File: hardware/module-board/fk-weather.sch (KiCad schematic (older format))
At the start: 68 parts, among them J1 MICRO-USB, J10 Conn_01x06, J11 Conn_01x06, J3 Conn_01x10, J6 CONN-HDR-2x5, M1 MOUNT_HOLE, M2 MOUNT_HOLE, M3 MOUNT_HOLE, M4 MOUNT_HOLE, Q1 2N7002LT1G, Q2 2N7002LT1G, Q3 2N7002LT1G, Q4 2N7002LT1G, Q5 2N7002LT1G, SW1 SPNO, U1 ATSAMD21G18A-AU, U2 MCP1700T-XXX2E, U4 S25FL1xxK0XM, Y1 FC-135

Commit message: Updating BOM details.
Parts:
- R34: spn1 603-RC0603FR-07330RL -> 603-AF0603JR-074K7L
- U4: spn1 (none) -> 797-25FL116KOXMFI041

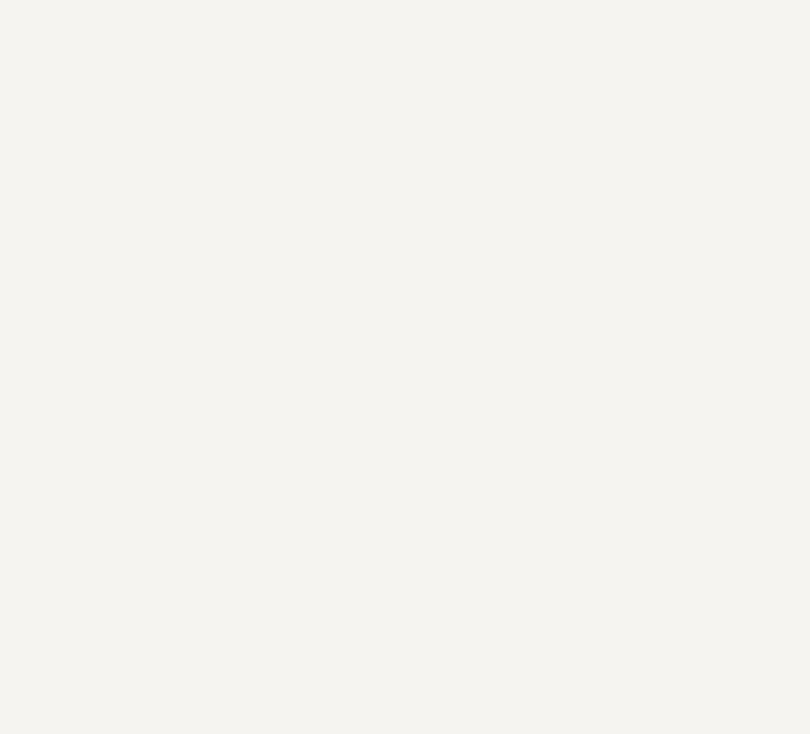
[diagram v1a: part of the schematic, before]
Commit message: Add connectors. Clean up mounting hole locations.
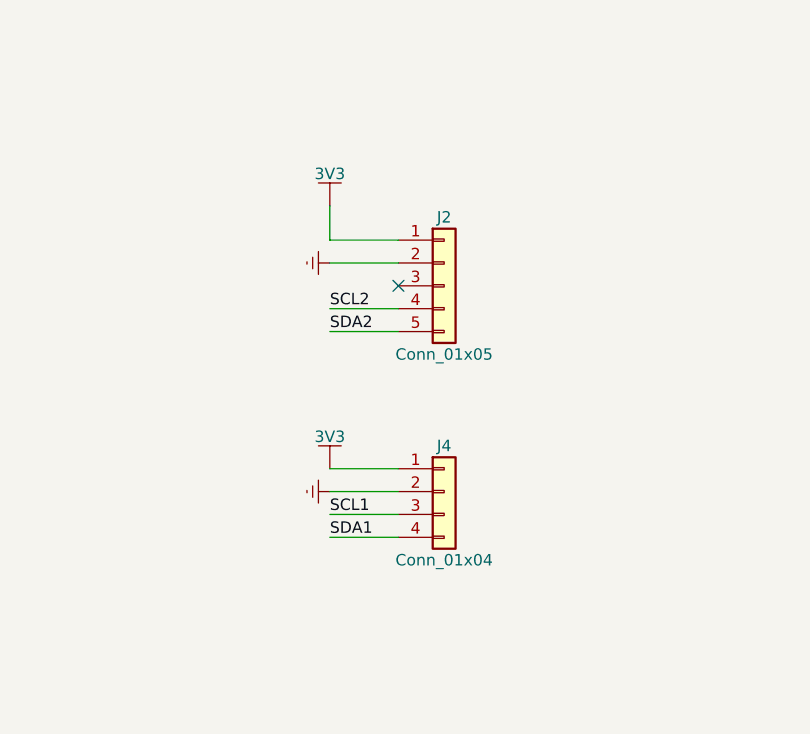
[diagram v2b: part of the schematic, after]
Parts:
- added J2: Conn_01x05, conservify:Molex_CLIK-Mate_502382-0570_1x05_P1.25mm_Vertical, symbol Conn_01x05
- added J4: Conn_01x04, conservify:Molex_CLIK-Mate_502382-0470_1x04_P1.25mm_Vertical, symbol Conn_01x04
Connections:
- wire segments 223 -> 232
- no-connect marks 6 -> 7

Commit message: Adding high side switch for peripherals.
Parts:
- removed Q5: 2N7002LT1G, RocketScreamKicadLibrary:SOT-23, symbol MOSFET-N
- added C13, C15: 100nF, RocketScreamKicadLibrary:CAP-0603, symbol CAPACITOR-CERAMIC
- added C16: 10uF, RocketScreamKicadLibrary:CAP-0603, symbol CAPACITOR-CERAMIC
- added J5: Conn_01x02, conservify:SJ_OPEN, symbol Conn_01x02
- added U3: TPS2041B, TO_SOT_Packages_SMD:SOT-23-5_HandSoldering, symbol TPS2041B
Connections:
- net labels added: PERIPH_3V3
- net labels removed: PERIPH_GND
- wire segments 232 -> 242

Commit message: Drop large header. Add debug. Drop LEDs.
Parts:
- removed D1: Orange, RocketScreamKicadLibrary:LED-0603, symbol LED-SINGLE
- removed D2: Yellow, RocketScreamKicadLibrary:LED-0603, symbol LED-SINGLE
- removed D3: Blue, RocketScreamKicadLibrary:LED-0603, symbol LED-SINGLE
- removed J3: Conn_01x10, Socket_Strips:Socket_Strip_Straight_1x10_Pitch2.54mm, symbol Conn_01x10
- removed J6: CONN-HDR-2x5, Socket_Strips:Socket_Strip_Straight_2x05_Pitch1.27mm_SMD, symbol CONN-HDR-2x5
- removed Q1, Q2, Q3: 2N7002LT1G, RocketScreamKicadLibrary:SOT-23, symbol MOSFET-N
- removed R1, R3, R5: 2k2, RocketScreamKicadLibrary:RES-0603, symbol RESISTOR
- removed R28, R29: 4.7K, RocketScreamKicadLibrary:RES-0603, symbol RESISTOR
- added J3: CONN_01x03_SERIAL, conservify:Molex_CLIK-Mate_502382-0370_1x03_P1.25mm_Vertical, symbol CONN_01x03_SERIAL
- added J6: CONN_02x05_SWD, conservify:HDR_02x05_Pitch1.27mm_SMD_SWD, symbol CONN_02x05_SWD
- C1, C10, C11, C12, C13, C14, C15, C16, C18, C2, C3, C4, C5, C6, C7, C8, C9: footprint RocketScreamKicadLibrary:CAP-0603 -> conservify:CAP-0603
- D10, D11, D6, D7, D8, D9: footprint RocketScreamKicadLibrary:SOD-123 -> conservify:SOD-123
- D4: footprint RocketScreamKicadLibrary:SOT-143B -> conservify:SOT-143B
- D5: footprint RocketScreamKicadLibrary:LED-0603 -> conservify:LED-0603
- F1: footprint RocketScreamKicadLibrary:MF-PSMF020X -> conservify:MF-PSMF020X
- L1, L2: footprint RocketScreamKicadLibrary:IND-0603 -> conservify:IND-0603
- M1, M2, M3, M4: footprint RocketScreamKicadLibrary:HOLE_NPTH_2.2MM -> conservify:HOLE_NPTH_2.54MM
- Q4: footprint RocketScreamKicadLibrary:SOT-23 -> conservify:SOT-23
- R10, R11, R17, R2, R22, R23, R30, R31, R32, R33, R34, R4, R6, R7, R8, R9: footprint RocketScreamKicadLibrary:RES-0603 -> conservify:RES-0603
- SW1: footprint RocketScreamKicadLibrary:TS-018 -> conservify:SW_SPST_WURTH_1
- U1: footprint RocketScreamKicadLibrary:TQFP-48_7x7mm_Pitch0.5mm -> conservify:TQFP-48_7x7mm_Pitch0.5mm
- U2: footprint RocketScreamKicadLibrary:SOT-89 -> conservify:SOT-89
- U3: footprint TO_SOT_Packages_SMD:SOT-23-5_HandSoldering -> conservify:SOT-23-5_HandSoldering
- U4: footprint RocketScreamKicadLibrary:SOIC-8-N -> conservify:SOIC-8-N
- Y1: footprint RocketScreamKicadLibrary:ABS07 -> conservify:ABS07
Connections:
- wire segments 242 -> 213
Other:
- note removed: "1.27 mm (0.05")"
- note removed: "M2.5 size"
- moved on the sheet: C13, C15, C16, J2, J4, J5, M1, M2, M3, M4, R11, R6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

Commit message: Add RTC. Molex connector cleanup. Add RGB LED.Fix diode footprints.
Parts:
- added BT1: BATTERY_CELL, conservify:BAT_CR1210, symbol BATTERY_CELL
- added C17, C19: 10nF, conservify:CAP-0603, symbol CAPACITOR-CERAMIC
- added R1: 1K, conservify:RES-0603, symbol RESISTOR
- added U5: SK6812, conservify:SK6812, symbol SK6812
- added U6: PCF8523, conservify:SOIC-8-N, symbol PCF8523
- added Y2: FC-135, conservify:ABS07, symbol CRYSTAL
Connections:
- wire segments 213 -> 233
- no-connect marks 7 -> 8
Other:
- note added: "CONNECTIONS"
- note added: "FLASH"
- note added: "I2C"
- note added: "LEDs\n"
- note added: "MCU"
- note added: "MOUNTING"
- note added: "PERIPHERALS"
- note added: "RAIN"
- note added: "RTC"
- note added: "USB / POWER MANAGEMENT"
- note added: "WIND"
- moved on the sheet: C1, C10, C11, C12, C13, C14, C15, C16, C18, C2, C3, C4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

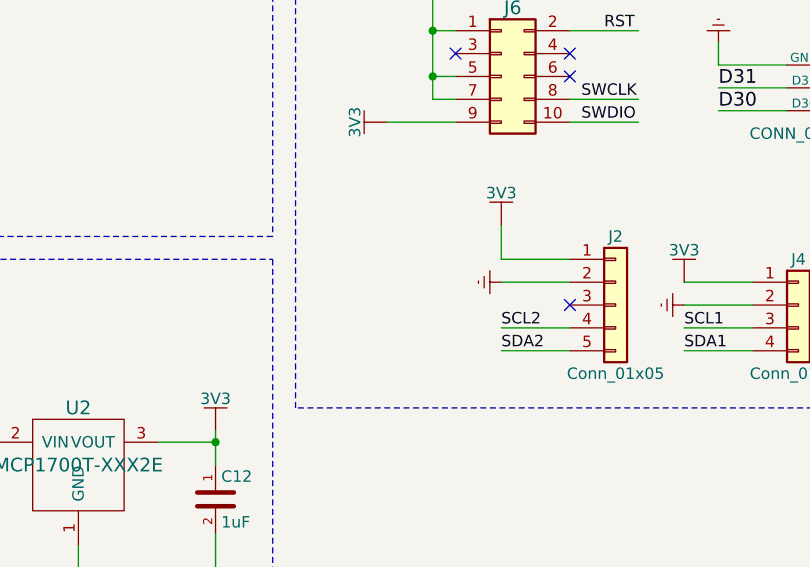
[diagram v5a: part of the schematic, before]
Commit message: Add a second core port.
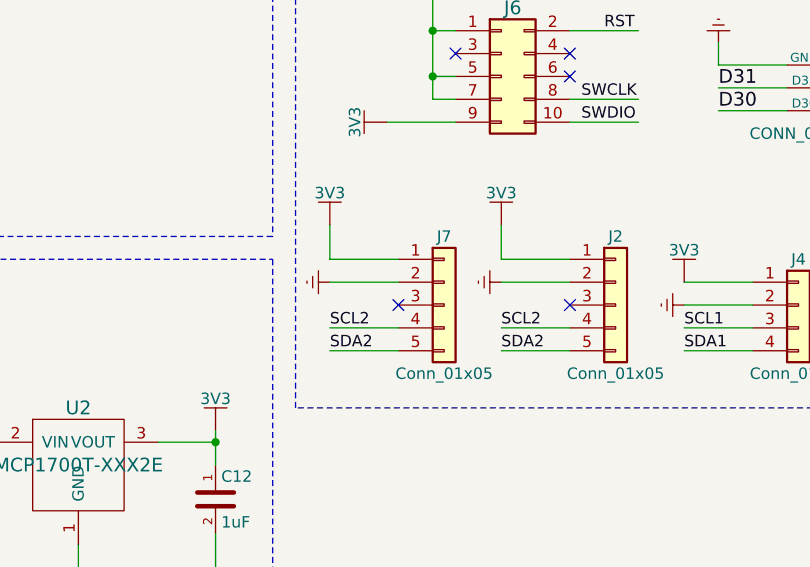
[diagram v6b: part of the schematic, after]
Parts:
- added J7: Conn_01x05, conservify:Molex_CLIK-Mate_502382-0570_1x05_P1.25mm_Vertical, symbol Conn_01x05
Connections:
- wire segments 233 -> 238
- no-connect marks 8 -> 9

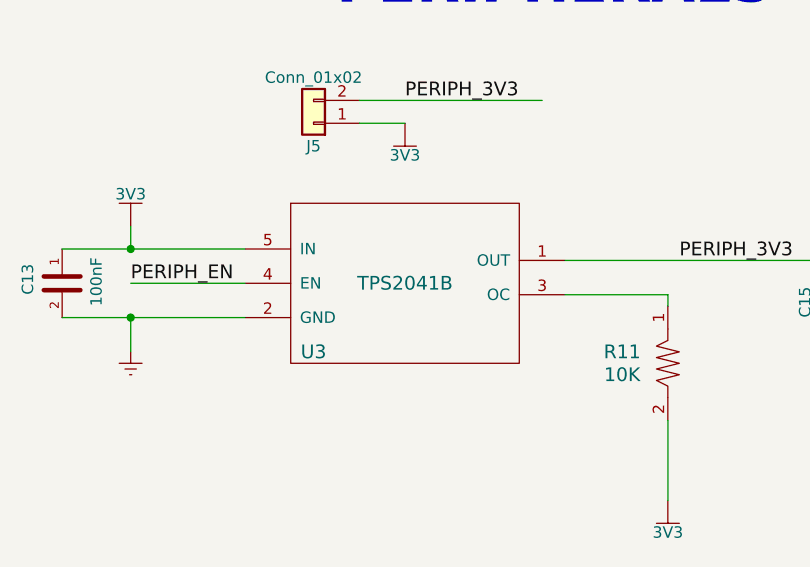
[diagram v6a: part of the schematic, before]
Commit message: Part for load switch was wrong, fixing.
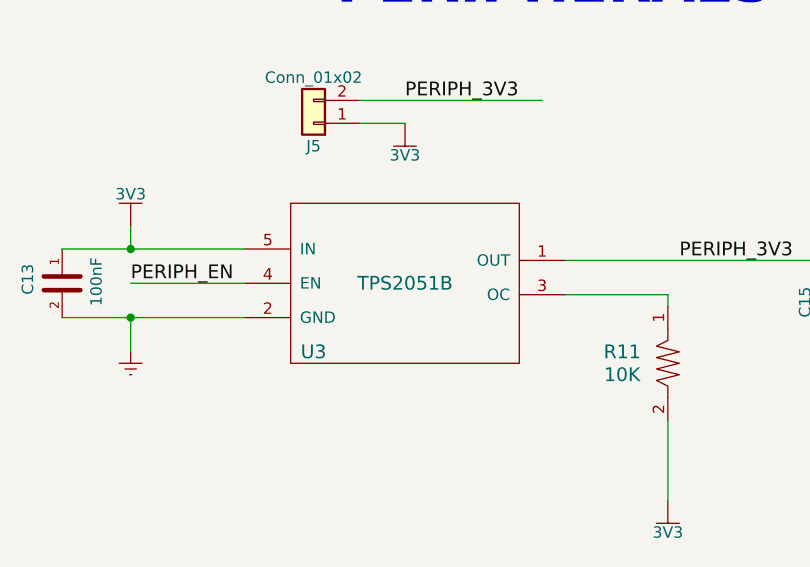
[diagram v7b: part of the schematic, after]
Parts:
- removed U3: TPS2041B, conservify:SOT-23-5_HandSoldering, symbol TPS2041B
- added U3: TPS2051B, conservify:SOT-23-5_HandSoldering, symbol TPS2051B
